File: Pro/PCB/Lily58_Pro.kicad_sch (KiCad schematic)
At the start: 83 parts, among them J1 LED, J2 4PIN, J3 OLED, P1 i2c_pin, P2 i2c_pin, SW1 SW_PUSH, SW10 SW_PUSH, SW11 SW_PUSH, SW12 SW_PUSH, SW13 SW_PUSH, SW14 SW_PUSH, SW15 SW_PUSH, SW16 SW_PUSH, SW17 SW_PUSH, SW18 SW_PUSH, SW19 SW_PUSH, SW2 SW_PUSH, SW20 SW_PUSH, SW21 SW_PUSH, SW22 SW_PUSH, SW23 SW_PUSH, SW24 SW_PUSH, SW25 SW_PUSH, SW26 SW_PUSH, SW27 SW_PUSH, SW28 SW_PUSH, SW29 SW_PUSH, SW3 SW_PUSH, SW4 SW_PUSH, SW5 SW_PUSH, SW6 SW_PUSH, SW7 SW_PUSH, SW8 SW_PUSH, SW9 SW_PUSH, U1 ProMicro

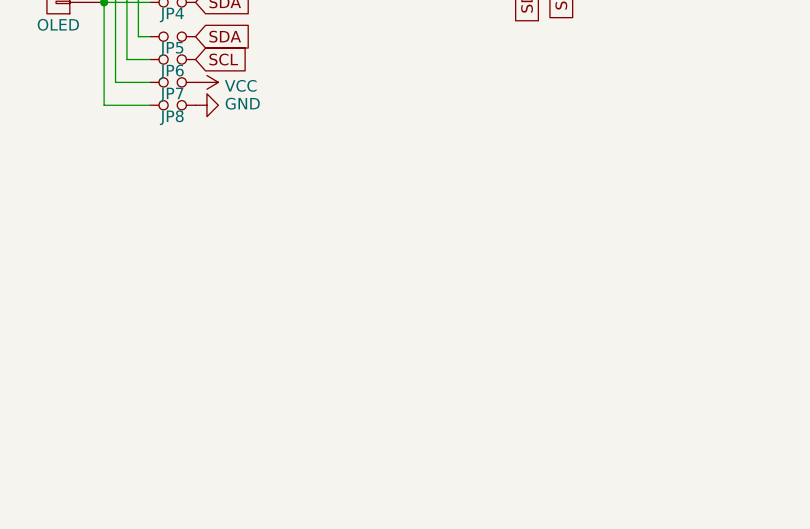
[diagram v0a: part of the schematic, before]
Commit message: Added power switch and JST-PH 2.0 connector for battery. Flooded islands and via stitched top and bottom ground planes.
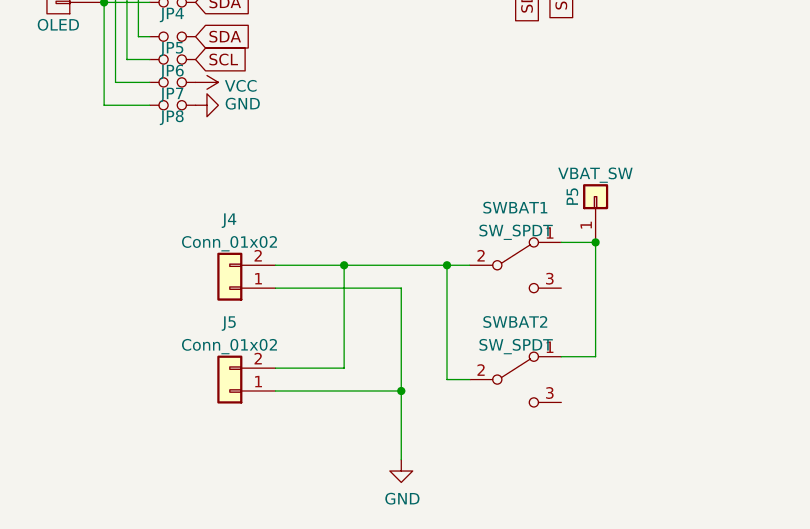
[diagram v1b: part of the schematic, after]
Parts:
- added J4, J5: Conn_01x02, Connector_JST:JST_PH_B2B-PH-K_1x02_P2.00mm_Vertical, symbol Connector_Generic:Conn_01x02
- added P5: VBAT_SW, Lily58_Pro-footprint:1pin_conn, symbol Lily58_Pro-rescue:i2c_pin-Lily58-cache
- added SWBAT1, SWBAT2: SW_SPDT, Button_Switch_SMD:SW_SPDT_PCM12, symbol Switch:SW_SPDT
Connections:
- net GND: now also J4.1 (Pin_1), J5.1 (Pin_1)
- new net: J4.2 (Pin_2), J5.2 (Pin_2), SWBAT1.2 (B), SWBAT2.2 (B)
- new net: P5.1 (Pin_1), SWBAT1.1 (A), SWBAT2.1 (A)
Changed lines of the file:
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@@
   (junction (at 160.02 90.17) (diameter 0) (color 0 0 0 0)
   )
+  (junction (at 119.38 160.02) (diameter 0) (color 0 0 0 0)
+  )
   (junction (at 236.22 97.79) (diameter 0) (color 0 0 0 0)
   )
@@
   (junction (at 160.02 106.68) (diameter 0) (color 0 0 0 0)
   )
+  (junction (at 102.87 162.56) (diameter 0) (color 0 0 0 0)
+  )
   (junction (at 200.66 73.66) (diameter 0) (color 0 0 0 0)
   )
@@
   (junction (at 175.26 114.3) (diameter 0) (color 0 0 0 0)
   )
+  (junction (at 91.44 162.56) (diameter 0) (color 0 0 0 0)
+  )
   (junction (at 215.9 130.81) (diameter 0) (color 0 0 0 0)
   )
@@
   (junction (at 90.17 115.57) (diameter 0) (color 0 0 0 0)
   )
+  (junction (at 97.79 176.53) (diameter 0) (color 0 0 0 0)
+  )
   (junction (at 215.9 114.3) (diameter 0) (color 0 0 0 0)
   )
@@
   (no_connect (at 64.77 68.58))
   (no_connect (at 97.79 53.34))
+  (wire (pts (xy 97.79 165.1) (xy 97.79 176.53))
+    (stroke (width 0) (type default))
+  )
+  (wire (pts (xy 105.41 175.26) (xy 102.87 175.26))
+    (stroke (width 0) (type default))
+  )
   (wire (pts (xy 64.77 144.78) (xy 69.85 144.78))
     (stroke (width 0) (type default))
@@
     (stroke (width 0) (type default))
   )
+  (wire (pts (xy 115.57 172.72) (xy 119.38 172.72))
+    (stroke (width 0) (type default))
+  )
   (wire (pts (xy 154.94 81.28) (xy 133.35 81.28))
     (stroke (width 0) (type default))
@@
     (stroke (width 0) (type default))
   )
+  (wire (pts (xy 91.44 162.56) (xy 102.87 162.56))
+    (stroke (width 0) (type default))
+  )
   (wire (pts (xy 195.58 81.28) (xy 215.9 81.28))
     (stroke (width 0) (type default))
@@
     (stroke (width 0) (type default))
   )
+  (wire (pts (xy 83.82 162.56) (xy 91.44 162.56))
+    (stroke (width 0) (type default))
+  )
   (wire (pts (xy 175.26 81.28) (xy 195.58 81.28))
     (stroke (width 0) (type default))
@@
     (stroke (width 0) (type default))
   )
+  (wire (pts (xy 97.79 176.53) (xy 97.79 184.15))
+    (stroke (width 0) (type default))
+  )
   (wire (pts (xy 195.58 130.81) (xy 215.9 130.81))
     (stroke (width 0) (type default))
@@
     (stroke (width 0) (type default))
   )
+  (wire (pts (xy 102.87 175.26) (xy 102.87 162.56))
+    (stroke (width 0) (type default))
+  )
   (wire (pts (xy 175.26 81.28) (xy 154.94 81.28))
     (stroke (width 0) (type default))
@@
     (stroke (width 0) (type default))
   )
+  (wire (pts (xy 83.82 165.1) (xy 97.79 165.1))
+    (stroke (width 0) (type default))
+  )
   (wire (pts (xy 241.3 90.17) (xy 241.3 73.66))
     (stroke (width 0) (type default))
@@
     (stroke (width 0) (type default))
   )
+  (wire (pts (xy 119.38 172.72) (xy 119.38 160.02))
+    (stroke (width 0) (type default))
+  )
   (wire (pts (xy 80.01 115.57) (xy 90.17 115.57))
     (stroke (width 0) (type default))
   )
+  (wire (pts (xy 102.87 162.56) (xy 105.41 162.56))
+    (stroke (width 0) (type default))
+  )
+  (wire (pts (xy 83.82 173.99) (xy 91.44 173.99))
+    (stroke (width 0) (type default))
+  )
+  (wire (pts (xy 115.57 160.02) (xy 119.38 160.02))
+    (stroke (width 0) (type default))
+  )
   (wire (pts (xy 67.31 139.7) (xy 69.85 139.7))
     (stroke (width 0) (type default))
@@
     (stroke (width 0) (type default))
   )
+  (wire (pts (xy 91.44 162.56) (xy 91.44 173.99))
+    (stroke (width 0) (type default))
+  )
   (wire (pts (xy 154.94 114.3) (xy 133.35 114.3))
     (stroke (width 0) (type default))
@@
     (stroke (width 0) (type default))
   )
+  (wire (pts (xy 83.82 176.53) (xy 97.79 176.53))
+    (stroke (width 0) (type default))
+  )
   (global_label "col0" (shape input) (at 97.79 68.58 0)
     (effects (font (size 1.27 1.27)) (justify left))
@@
         )
       )
+    )
+  )
+  (symbol (lib_id "Connector_Generic:Conn_01x02") (at 78.74 176.53 180) (unit 1)
+    (in_bom yes) (on_board yes) (dnp no) (fields_autoplaced)
+    (property "Reference" "J5" (at 78.74 168.91 0)
+      (effects (font (size 1.27 1.27)))
+    )
+    (property "Value" "Conn_01x02" (at 78.74 171.45 0)
+      (effects (font (size 1.27 1.27)))
+    )
+    (property "Footprint" "Connector_JST:JST_PH_B2B-PH-K_1x02_P2.00mm_Vertical" (at 78.74 176.53 0)
+      (effects (font (size 1.27 1.27)) hide)
+    )
+    (property "Datasheet" "~" (at 78.74 176.53 0)
+      (effects (font (size 1.27 1.27)) hide)
+    )
+    (pin "1")
+    (pin "2")
+    (instances
+      (project "Lily58_Pro"
+        (path "/a39df9ba-6b06-463d-bd14-76d9cbe6e71e"
+          (reference "J5") (unit 1)
+        )
+      )
+    )
+  )
+  (symbol (lib_id "Lily58_Pro-rescue:GND-Lily58-cache") (at 97.79 184.15 0) (unit 1)
+    (in_bom yes) (on_board yes) (dnp no)
+    (property "Reference" "#PWR015" (at 97.79 190.5 0)
+      (effects (font (size 1.27 1.27)) hide)
+    )
+    (property "Value" "GND" (at 97.917 188.5442 0)
+      (effects (font (size 1.27 1.27)))
+    )
+    (property "Footprint" "" (at 97.79 184.15 0)
+      (effects (font (size 1.27 1.27)) hide)
+    )
+    (property "Datasheet" "" (at 97.79 184.15 0)
+      (effects (font (size 1.27 1.27)) hide)
+    )
+    (pin "1")
+    (instances
+      (project "Lily58_Pro"
+        (path "/a39df9ba-6b06-463d-bd14-76d9cbe6e71e"
+          (reference "#PWR015") (unit 1)
+        )
+      )
+    )
+  )
+  (symbol (lib_id "Switch:SW_SPDT") (at 110.49 162.56 0) (unit 1)
+    (in_bom yes) (on_board yes) (dnp no) (fields_autoplaced)
+    (property "Reference" "SWBAT1" (at 110.49 156.21 0)
+      (effects (font (size 1.27 1.27)))
+    )
+    (property "Value" "SW_SPDT" (at 110.49 158.75 0)
+      (effects (font (size 1.27 1.27)))
+    )
+    (property "Footprint" "Button_Switch_SMD:SW_SPDT_PCM12" (at 110.49 162.56 0)
+      (effects (font (size 1.27 1.27)) hide)
+    )
+    (property "Datasheet" "~" (at 110.49 162.56 0)
+      (effects (font (size 1.27 1.27)) hide)
+    )
+    (pin "1")
+    (pin "2")
+    (pin "3")
+    (instances
+      (project "Lily58_Pro"
+        (path "/a39df9ba-6b06-463d-bd14-76d9cbe6e71e"
+          (reference "SWBAT1") (unit 1)
+        )
+      )
+    )
+  )
+  (symbol (lib_id "Connector_Generic:Conn_01x02") (at 78.74 165.1 180) (unit 1)
+    (in_bom yes) (on_board yes) (dnp no) (fields_autoplaced)
+    (property "Reference" "J4" (at 78.74 157.48 0)
+      (effects (font (size 1.27 1.27)))
+    )
+    (property "Value" "Conn_01x02" (at 78.74 160.02 0)
+      (effects (font (size 1.27 1.27)))
+    )
+    (property "Footprint" "Connector_JST:JST_PH_B2B-PH-K_1x02_P2.00mm_Vertical" (at 78.74 165.1 0)
+      (effects (font (size 1.27 1.27)) hide)
+    )
+    (property "Datasheet" "~" (at 78.74 165.1 0)
+      (effects (font (size 1.27 1.27)) hide)
+    )
+    (pin "1")
+    (pin "2")
+    (instances
+      (project "Lily58_Pro"
+        (path "/a39df9ba-6b06-463d-bd14-76d9cbe6e71e"
+          (reference "J4") (unit 1)
+        )
+      )
+    )
+  )
+  (symbol (lib_id "Switch:SW_SPDT") (at 110.49 175.26 0) (unit 1)
+    (in_bom yes) (on_board yes) (dnp no) (fields_autoplaced)
+    (property "Reference" "SWBAT2" (at 110.49 168.91 0)
+      (effects (font (size 1.27 1.27)))
+    )
+    (property "Value" "SW_SPDT" (at 110.49 171.45 0)
+      (effects (font (size 1.27 1.27)))
+    )
+    (property "Footprint" "Button_Switch_SMD:SW_SPDT_PCM12" (at 110.49 175.26 0)
+      (effects (font (size 1.27 1.27)) hide)
+    )
+    (property "Datasheet" "~" (at 110.49 175.26 0)
+      (effects (font (size 1.27 1.27)) hide)
+    )
+    (pin "1")
+    (pin "2")
+    (pin "3")
+    (instances
+      (project "Lily58_Pro"
+        (path "/a39df9ba-6b06-463d-bd14-76d9cbe6e71e"
+          (reference "SWBAT2") (unit 1)
+        )
+      )
+    )
+  )
+  (symbol (lib_id "Lily58_Pro-rescue:i2c_pin-Lily58-cache") (at 119.38 154.94 90) (unit 1)
+    (in_bom yes) (on_board yes) (dnp no)
+    (property "Reference" "P5" (at 116.84 154.94 0)
+      (effects (font (size 1.27 1.27)))
+    )
+    (property "Value" "VBAT_SW" (at 119.38 152.4 90)
+      (effects (font (size 1.27 1.27)))
+    )
+    (property "Footprint" "Lily58_Pro-footprint:1pin_conn" (at 119.38 154.94 0)
+      (effects (font (size 1.27 1.27)) hide)
+    )
+    (property "Datasheet" "" (at 119.38 154.94 0)
+      (effects (font (size 1.27 1.27)) hide)
+    )
+    (pin "1")
+    (instances
+      (project "Lily58_Pro"
+        (path "/a39df9ba-6b06-463d-bd14-76d9cbe6e71e"
+          (reference "P5") (unit 1)
+        )
+      )

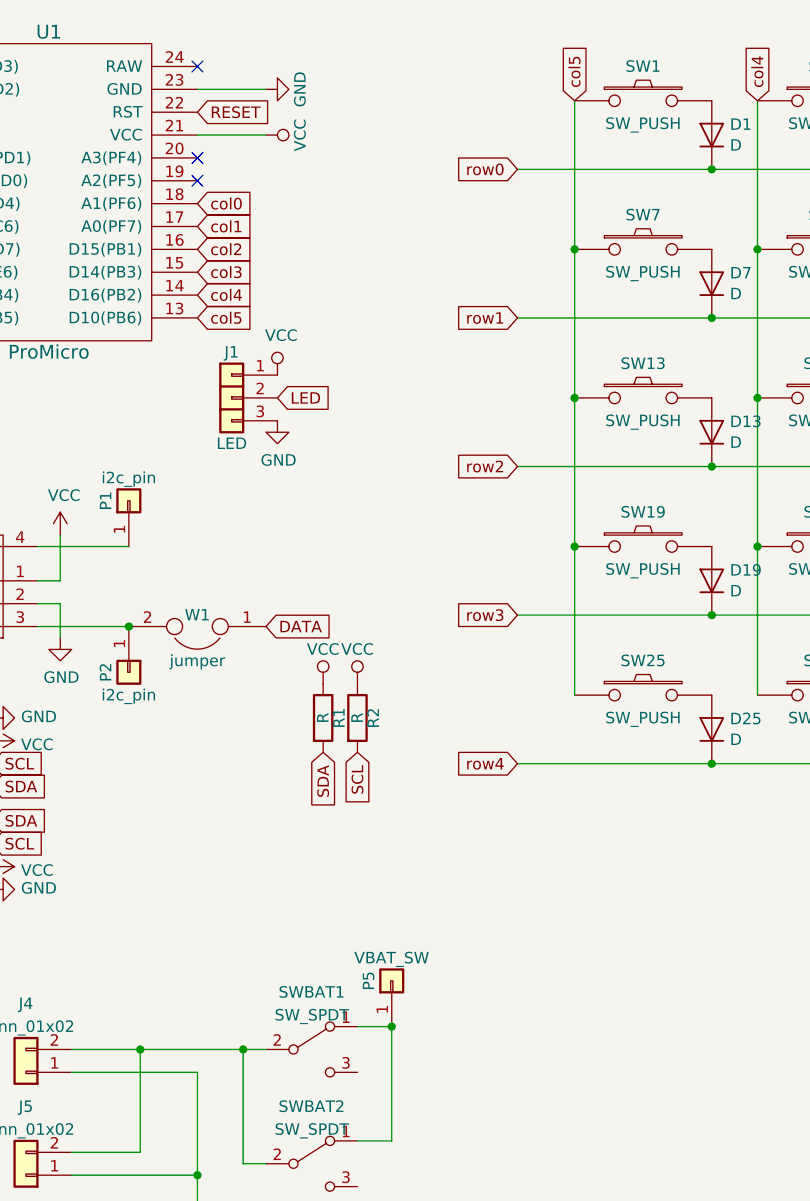
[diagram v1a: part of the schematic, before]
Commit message: Added connection from VBAT_SW to RAW pin on nano socket (for Nice!Nano)
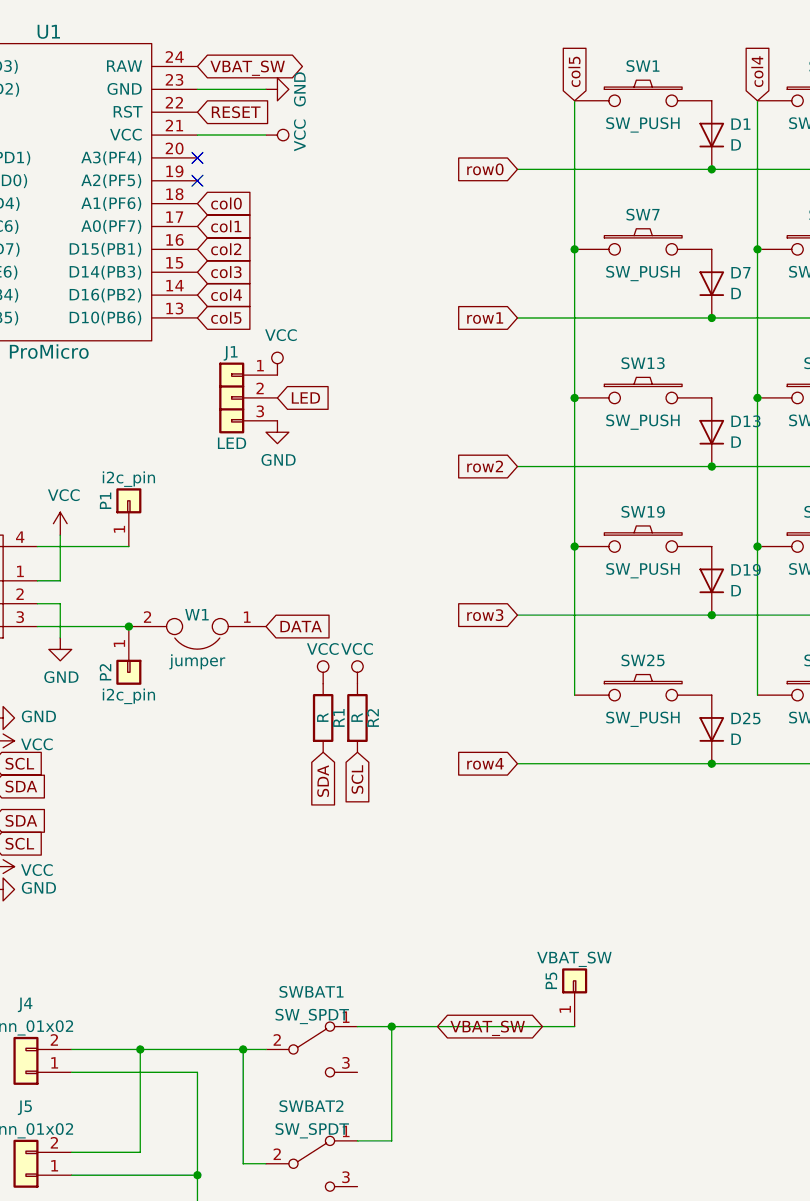
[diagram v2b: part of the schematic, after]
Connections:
- net VBAT_SW: now reaches U1.24 (RAW)
- net VBAT_SW: now also P5.1 (Pin_1), SWBAT1.1 (A), SWBAT2.1 (A)
- no-connect marks 4 -> 3
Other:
- moved on the sheet: P5
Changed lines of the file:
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@@
   (no_connect (at 97.79 66.04))
   (no_connect (at 64.77 68.58))
-  (no_connect (at 97.79 53.34))
   (wire (pts (xy 97.79 165.1) (xy 97.79 176.53))
     (stroke (width 0) (type default))
@@
     (stroke (width 0) (type default))
   )
+  (wire (pts (xy 139.7 160.02) (xy 119.38 160.02))
+    (stroke (width 0) (type default))
+  )
   (wire (pts (xy 180.34 57.15) (xy 180.34 73.66))
     (stroke (width 0) (type default))
@@
     )
   )
+  (global_label "VBAT_SW" (shape bidirectional) (at 124.46 160.02 0) (fields_autoplaced)
+    (effects (font (size 1.27 1.27)) (justify left))
+    (property "Intersheetrefs" "${INTERSHEET_REFS}" (at 135.7074 160.02 0)
+      (effects (font (size 1.27 1.27)) (justify left) hide)
+    )
+  )
   (global_label "row4" (shape input) (at 64.77 81.28 180)
     (effects (font (size 1.27 1.27)) (justify right))
@@
     )
   )
+  (global_label "VBAT_SW" (shape bidirectional) (at 97.79 53.34 0) (fields_autoplaced)
+    (effects (font (size 1.27 1.27)) (justify left))
+    (property "Intersheetrefs" "${INTERSHEET_REFS}" (at 109.0374 53.34 0)
+      (effects (font (size 1.27 1.27)) (justify left) hide)
+    )
+  )
   (global_label "SCL" (shape input) (at 64.77 66.04 180)
     (effects (font (size 1.27 1.27)) (justify right))
@@
     )
   )
-  (symbol (lib_id "Lily58_Pro-rescue:i2c_pin-Lily58-cache") (at 119.38 154.94 90) (unit 1)
+  (symbol (lib_id "Lily58_Pro-rescue:i2c_pin-Lily58-cache") (at 139.7 154.94 90) (unit 1)
     (in_bom yes) (on_board yes) (dnp no)
-    (property "Reference" "P5" (at 116.84 154.94 0)
+    (property "Reference" "P5" (at 137.16 154.94 0)
       (effects (font (size 1.27 1.27)))
     )
-    (property "Value" "VBAT_SW" (at 119.38 152.4 90)
+    (property "Value" "VBAT_SW" (at 139.7 152.4 90)
       (effects (font (size 1.27 1.27)))
     )
-    (property "Footprint" "Lily58_Pro-footprint:1pin_conn" (at 119.38 154.94 0)
+    (property "Footprint" "Lily58_Pro-footprint:1pin_conn" (at 139.7 154.94 0)
       (effects (font (size 1.27 1.27)) hide)
     )
-    (property "Datasheet" "" (at 119.38 154.94 0)
+    (property "Datasheet" "" (at 139.7 154.94 0)
       (effects (font (size 1.27 1.27)) hide)
     )

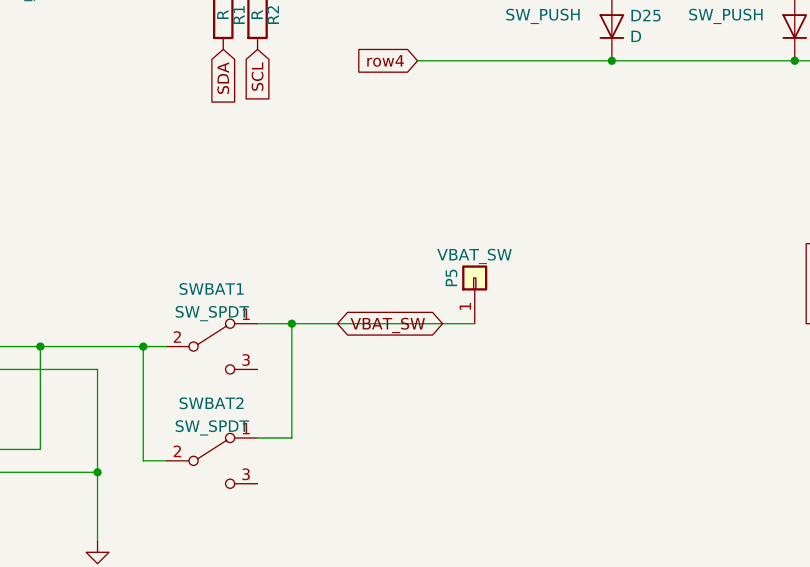
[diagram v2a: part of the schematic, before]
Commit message: Minor cosmetic updates to PCB
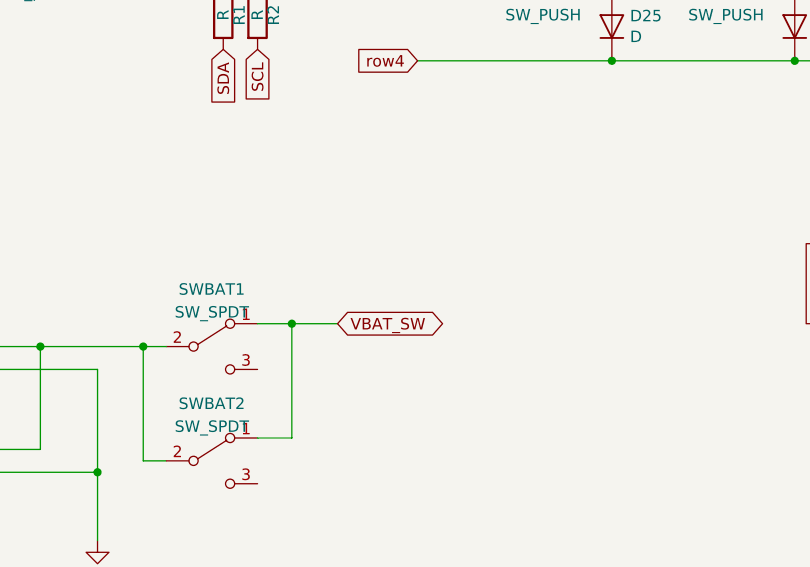
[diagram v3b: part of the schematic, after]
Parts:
- removed P5: VBAT_SW, Lily58_Pro-footprint:1pin_conn, symbol Lily58_Pro-rescue:i2c_pin-Lily58-cache
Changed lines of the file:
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@@
   (junction (at 160.02 90.17) (diameter 0) (color 0 0 0 0)
   )
-  (junction (at 119.38 160.02) (diameter 0) (color 0 0 0 0)
-  )
   (junction (at 236.22 97.79) (diameter 0) (color 0 0 0 0)
   )
@@
   (junction (at 175.26 81.28) (diameter 0) (color 0 0 0 0)
   )
+  (junction (at 119.38 160.02) (diameter 0) (color 0 0 0 0)
+  )
   (junction (at 175.26 130.81) (diameter 0) (color 0 0 0 0)
   )
@@
     (stroke (width 0) (type default))
   )
-  (wire (pts (xy 139.7 160.02) (xy 119.38 160.02))
-    (stroke (width 0) (type default))
-  )
   (wire (pts (xy 180.34 57.15) (xy 180.34 73.66))
     (stroke (width 0) (type default))
@@
     (stroke (width 0) (type default))
   )
+  (wire (pts (xy 119.38 160.02) (xy 124.46 160.02))
+    (stroke (width 0) (type default))
+  )
   (wire (pts (xy 80.01 106.68) (xy 90.17 106.68))
     (stroke (width 0) (type default))
@@
         )
       )
-    )
-  )
-  (symbol (lib_id "Lily58_Pro-rescue:i2c_pin-Lily58-cache") (at 139.7 154.94 90) (unit 1)
-    (in_bom yes) (on_board yes) (dnp no)
-    (property "Reference" "P5" (at 137.16 154.94 0)
-      (effects (font (size 1.27 1.27)))
-    )
-    (property "Value" "VBAT_SW" (at 139.7 152.4 90)
-      (effects (font (size 1.27 1.27)))
-    )
-    (property "Footprint" "Lily58_Pro-footprint:1pin_conn" (at 139.7 154.94 0)
-      (effects (font (size 1.27 1.27)) hide)
-    )
-    (property "Datasheet" "" (at 139.7 154.94 0)
-      (effects (font (size 1.27 1.27)) hide)
-    )
-    (pin "1")
-    (instances
-      (project "Lily58_Pro"
-        (path "/a39df9ba-6b06-463d-bd14-76d9cbe6e71e"
-          (reference "P5") (unit 1)
-        )
-      )

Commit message: KiCad 8.0 as ordered 2024-05-22 20:50
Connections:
- net DATA: now also J2.3, P2.1 (Pin_1), W1.2
